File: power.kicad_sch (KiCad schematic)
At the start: 31 parts, among them J3 Barrel_Jack, U4 TPS79933, U5 AP64501

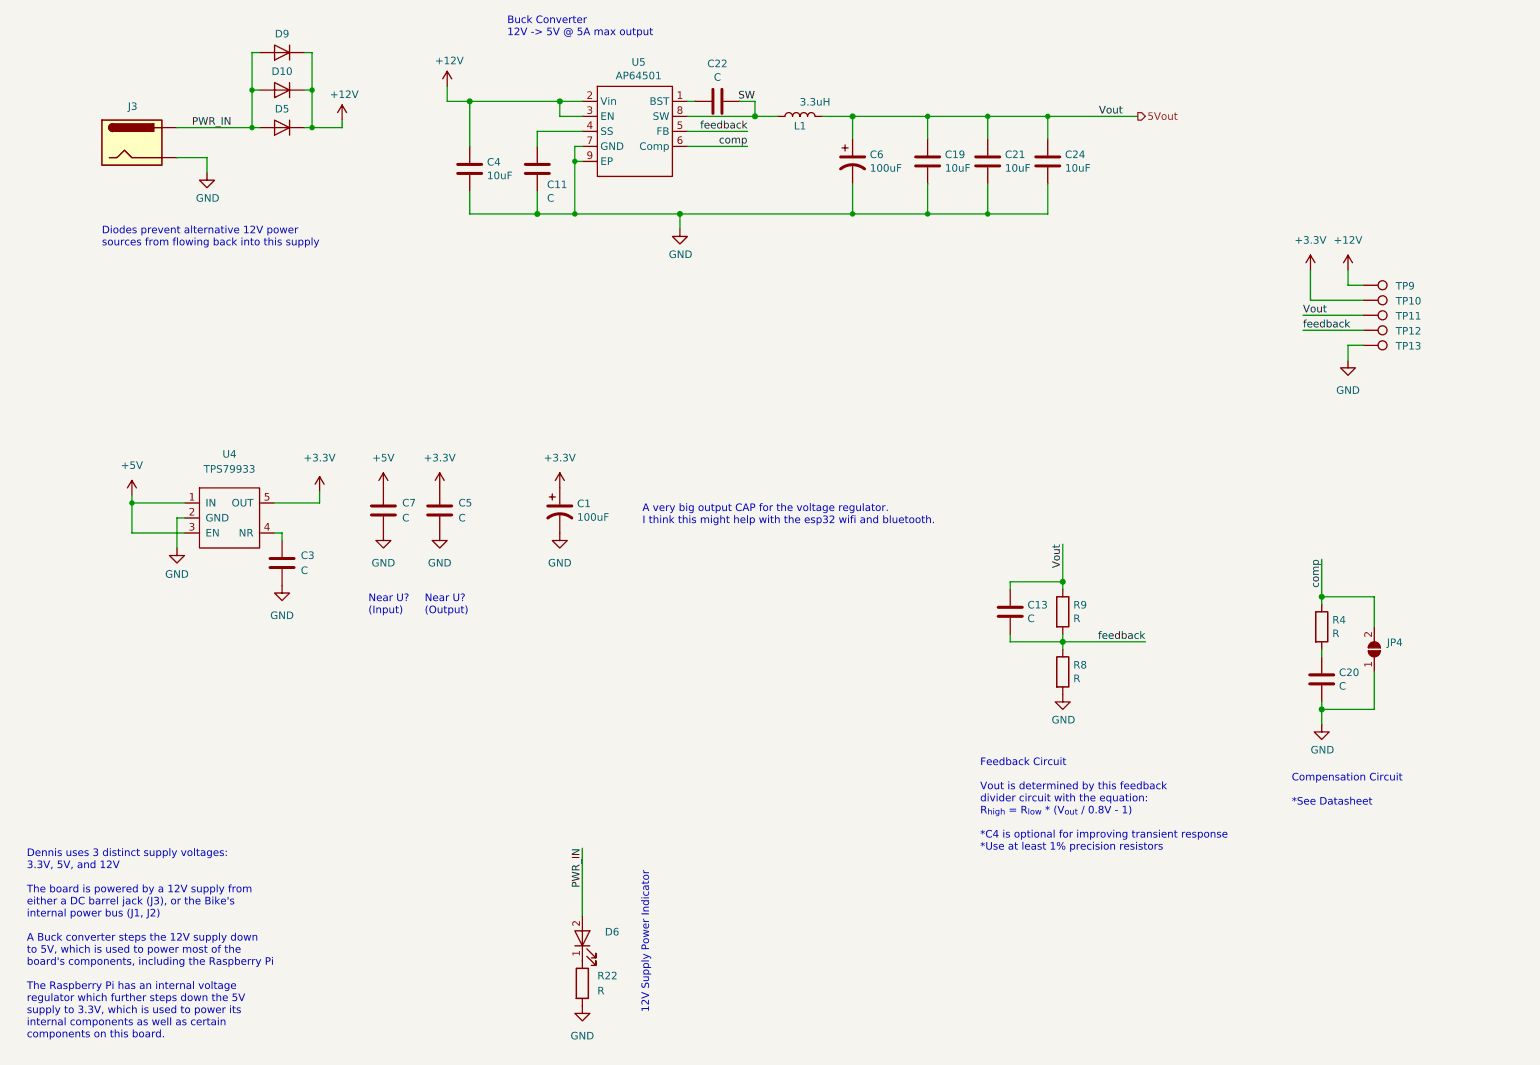
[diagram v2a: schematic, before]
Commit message: cleaned up schematic
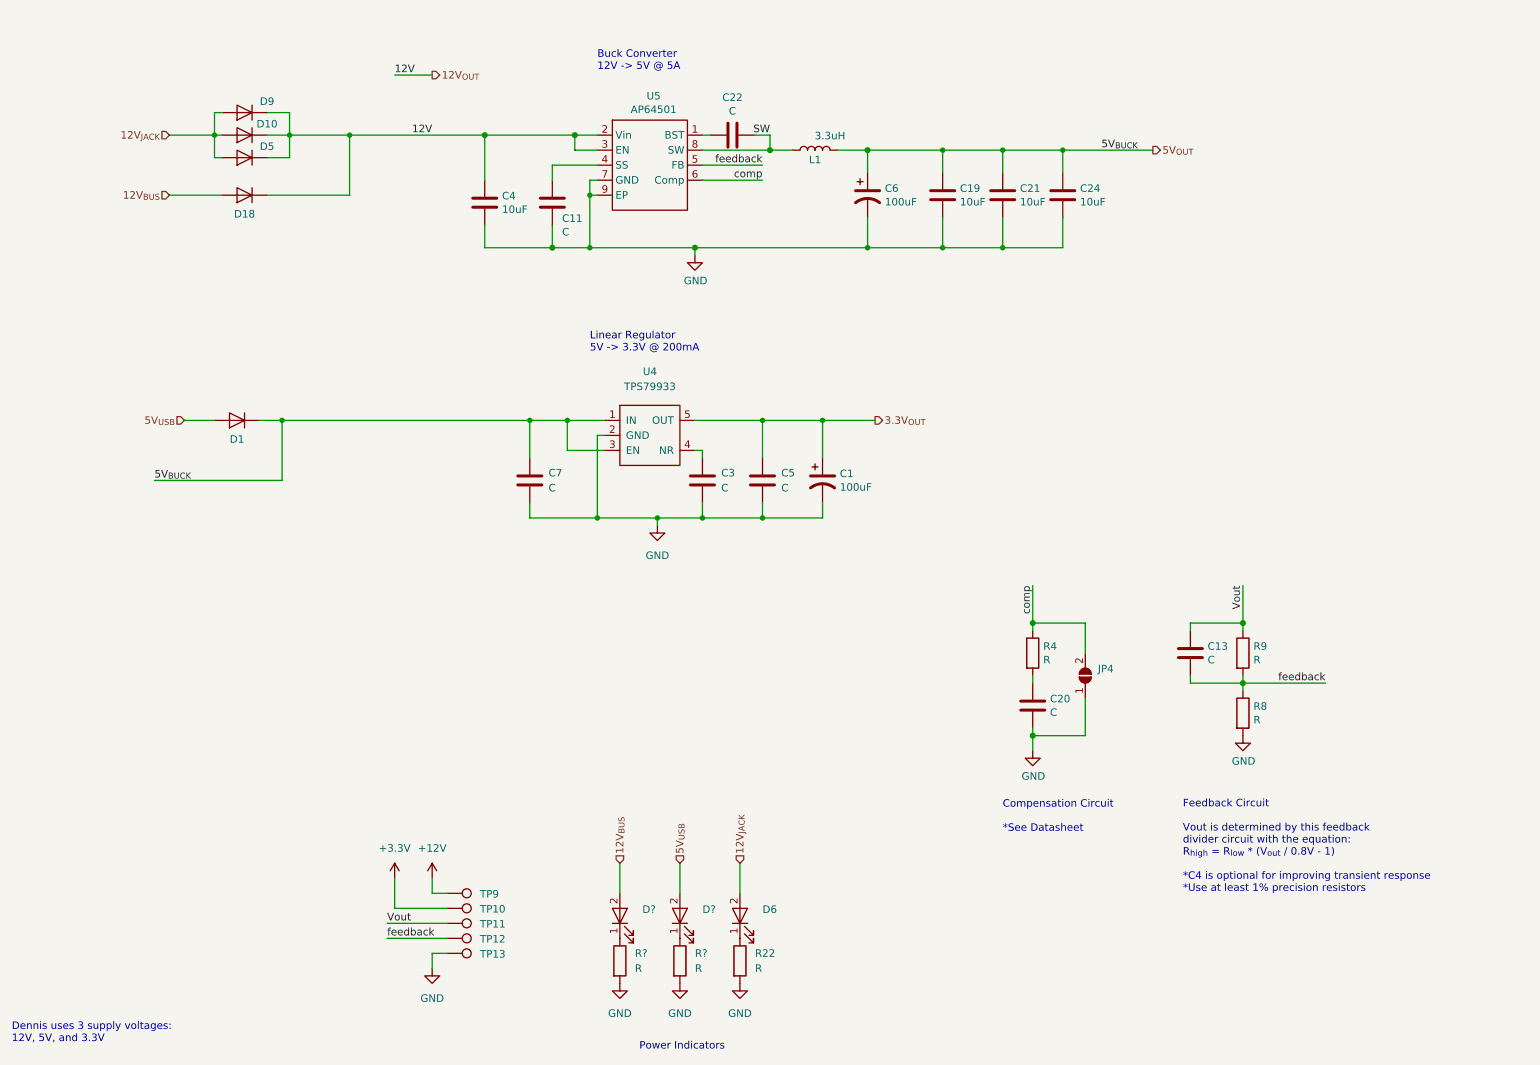
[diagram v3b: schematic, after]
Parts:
- removed J3: Barrel_Jack, Connector_BarrelJack:BarrelJack_Horizontal, symbol symbols:Barrel_Jack
- added D1, D18: Diode, Diode_SMD:D_SOD-123F, symbol symbols:Diode
- added D? (x2): LED_Green, LED_SMD:LED_0805_2012Metric_Pad1.15x1.40mm_HandSolder, symbol ecafe-racer:LED_Green
- added R? (x2): R, Resistor_SMD:R_0805_2012Metric, symbol Device:R
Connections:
- net +12V: no longer C4.1, D10.1 (K), D5.1 (K), D9.1 (K), U5.2 (Vin), U5.3 (EN)
- net +3V3: no longer C1.1, C5.1, U4.5 (OUT)
- net GND: now also R?.2, R?.2
- net +5V renamed 5V_{OUT}
- net 5V_{OUT}: now also C19.1, C21.1, C24.1, C6.1, L1.2, D1.1 (K)
- removed net 5Vout: C13.1, C19.1, C21.1, C24.1, C6.1, L1.2, R9.1, TP11.1
- net PWR_IN renamed 12V_{JACK}
- new net: D?.1, R?.1 (x2)
- new net 12V_{BUS}: D18.2 (A), D?.2
- new net 12V_{OUT}: C4.1, D10.1 (K), D18.1 (K), D5.1 (K), D9.1 (K), U5.2 (Vin), U5.3 (EN)
- new net 3.3V_{OUT}: C1.1, C5.1, U4.5 (OUT)
- new net 5V_{USB}: D1.2 (A), D?.2
- new net Vout: C13.1, R9.1, TP11.1
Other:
- note added: "Buck Converter 12V -> 5V @ 5A"
- note added: "Dennis uses 3 supply voltages: 12V, 5V, and 3.3V"
- note added: "Linear Regulator 5V -> 3.3V @ 200mA"
- note added: "Power Indicators"
- note removed: "12V Supply Power Indicator"
- note removed: "A very big output CAP for the voltage regulator. I think this might help with the esp32 wifi and bluetooth."
- note removed: "Buck Converter 12V -> 5V @ 5A max output"
- note removed: "Dennis uses 3 distinct supply voltages: 3.3V, 5V, and 12V The board is powered by a 12V supply from either a DC barrel jack (J3), or the Bike's internal power bus (J1, J2) A Buck converter steps the 12V supply down to 5V, which is used to power most of the board's components, including the Raspberry Pi The Raspberry Pi has an internal voltage regulator which further steps down the 5V supply to 3.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"
- note removed: "Diodes prevent alternative 12V power sources from flowing back into this supply"
- note removed: "Near U? (Input)"
- note removed: "Near U? (Output)"
- moved on the sheet: C1, C11, C13, C19, C20, C21, C22, C24, C3, C4, C5, C6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

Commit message: Forgot to connect the interrupt signal for the GPIO
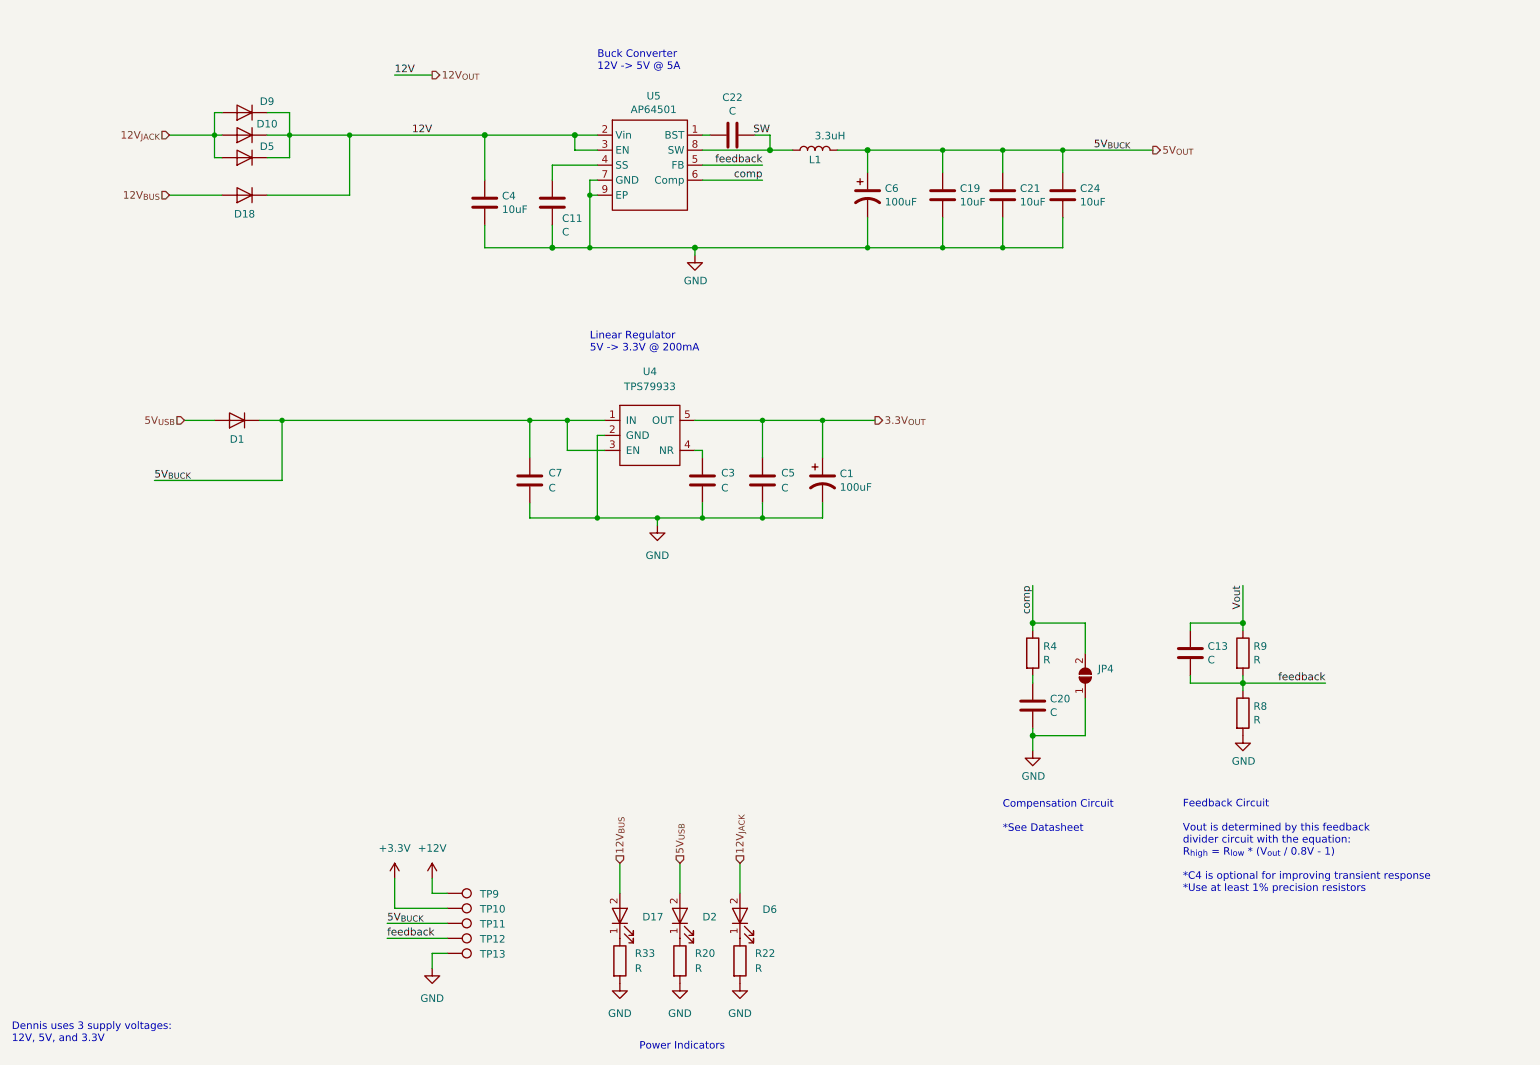
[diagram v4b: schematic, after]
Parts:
- gave numbers to parts that had none: 4
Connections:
- net 5V_{OUT}: now also TP11.1
- net Vout: no longer TP11.1
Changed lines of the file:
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@@
   (title_block
     (title "Dennis")
-    (date "2021-03-30")
+    (date "2021-08-07")
     (rev "0.2.1")
     (company "eCafe Racer")
@@
     (effects (font (size 1.27 1.27)) (justify left bottom))
   )
-  (label "Vout" (at 80.01 177.8 0)
+  (label "5V_{BUCK}" (at 80.01 177.8 0)
     (effects (font (size 1.27 1.27)) (justify left bottom))
   )
@@
     (effects (font (size 1.27 1.27)) (justify right bottom))
   )
-  (label "5V_{BUCK}" (at 207.01 46.99 180)
+  (label "5V_{BUCK}" (at 205.74 46.99 180)
     (effects (font (size 1.27 1.27)) (justify right bottom))
   )
@@
   (symbol (lib_id "power:GND") (at 119.38 187.96 0) (unit 1)
     (in_bom yes) (on_board yes) (fields_autoplaced)
-    (property "Reference" "#PWR?" (id 0) (at 119.38 194.31 0)
+    (property "Reference" "#PWR0115" (id 0) (at 119.38 194.31 0)
       (effects (font (size 1.27 1.27)) hide)
     )
@@
   (symbol (lib_id "power:GND") (at 125.73 110.49 0) (unit 1)
     (in_bom yes) (on_board yes) (fields_autoplaced)
-    (property "Reference" "#PWR?" (id 0) (at 125.73 116.84 0)
+    (property "Reference" "#PWR0121" (id 0) (at 125.73 116.84 0)
       (effects (font (size 1.27 1.27)) hide)
     )
@@
   (symbol (lib_id "power:GND") (at 129.54 187.96 0) (unit 1)
     (in_bom yes) (on_board yes) (fields_autoplaced)
-    (property "Reference" "#PWR?" (id 0) (at 129.54 194.31 0)
+    (property "Reference" "#PWR0111" (id 0) (at 129.54 194.31 0)
       (effects (font (size 1.27 1.27)) hide)
     )
@@
   (symbol (lib_id "Device:R") (at 119.38 184.15 0) (unit 1)
     (in_bom yes) (on_board yes) (fields_autoplaced)
-    (property "Reference" "R?" (id 0) (at 121.92 182.8799 0)
+    (property "Reference" "R33" (id 0) (at 121.92 182.8799 0)
       (effects (font (size 1.27 1.27)) (justify left))
     )
@@
   (symbol (lib_id "Device:R") (at 129.54 184.15 0) (unit 1)
     (in_bom yes) (on_board yes) (fields_autoplaced)
-    (property "Reference" "R?" (id 0) (at 132.08 182.8799 0)
+    (property "Reference" "R20" (id 0) (at 132.08 182.8799 0)
       (effects (font (size 1.27 1.27)) (justify left))
     )
@@
   (symbol (lib_id "ecafe-racer:LED_Green") (at 119.38 176.53 90) (unit 1)
     (in_bom yes) (on_board yes) (fields_autoplaced)
-    (property "Reference" "D?" (id 0) (at 123.19 175.4504 90)
+    (property "Reference" "D17" (id 0) (at 123.19 176.7204 90)
       (effects (font (size 1.27 1.27)) (justify right))
     )
@@
   (symbol (lib_id "ecafe-racer:LED_Green") (at 129.54 176.53 90) (unit 1)
     (in_bom yes) (on_board yes) (fields_autoplaced)
-    (property "Reference" "D?" (id 0) (at 133.35 175.4504 90)
+    (property "Reference" "D2" (id 0) (at 133.35 176.7204 90)
       (effects (font (size 1.27 1.27)) (justify right))
     )
